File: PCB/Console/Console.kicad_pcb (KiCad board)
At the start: 2 copper layers, 9 parts, among them J1 Conn_01x04_Socket, J2 Conn_01x02_Socket, J3 Conn_01x08_Socket, J4 Conn_01x06, U1 WeMos D1 Mini32

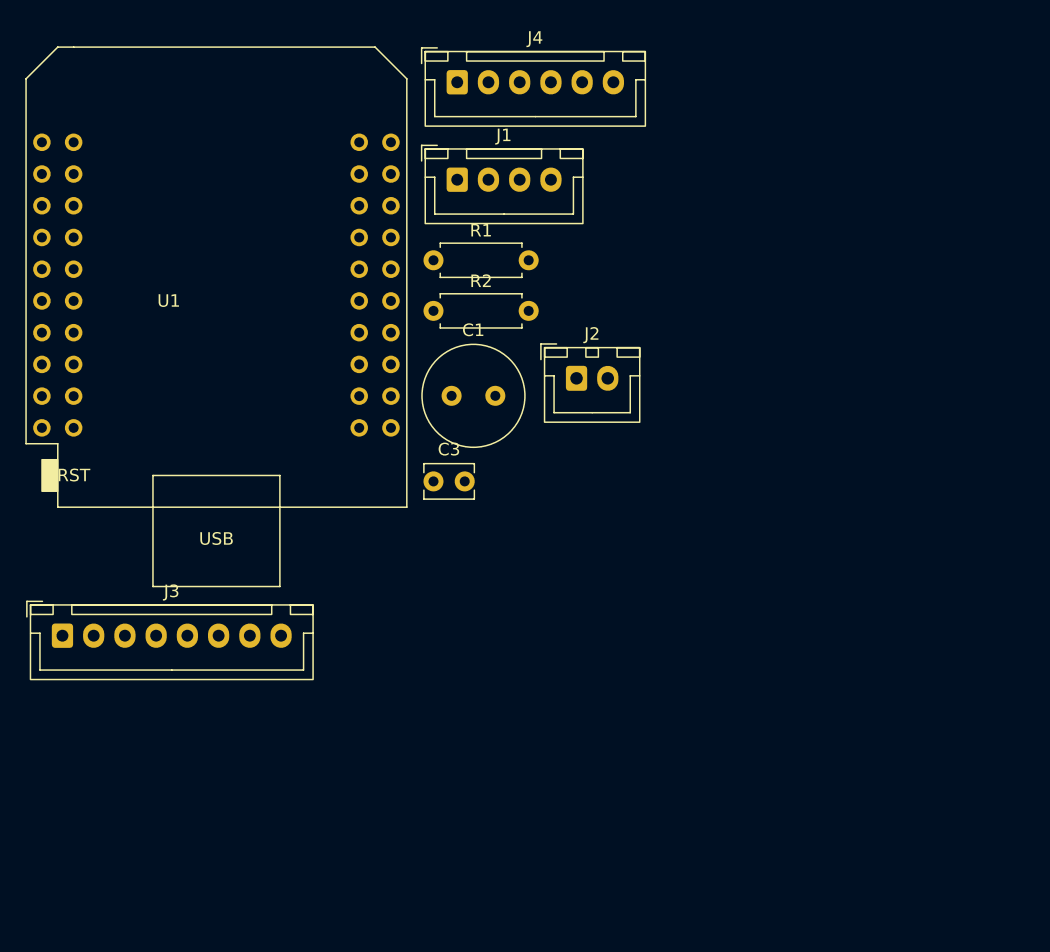
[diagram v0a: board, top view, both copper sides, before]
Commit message: Console: swap Waveshare pigtail for M128 7-pin socket (J3); F8 to PCB
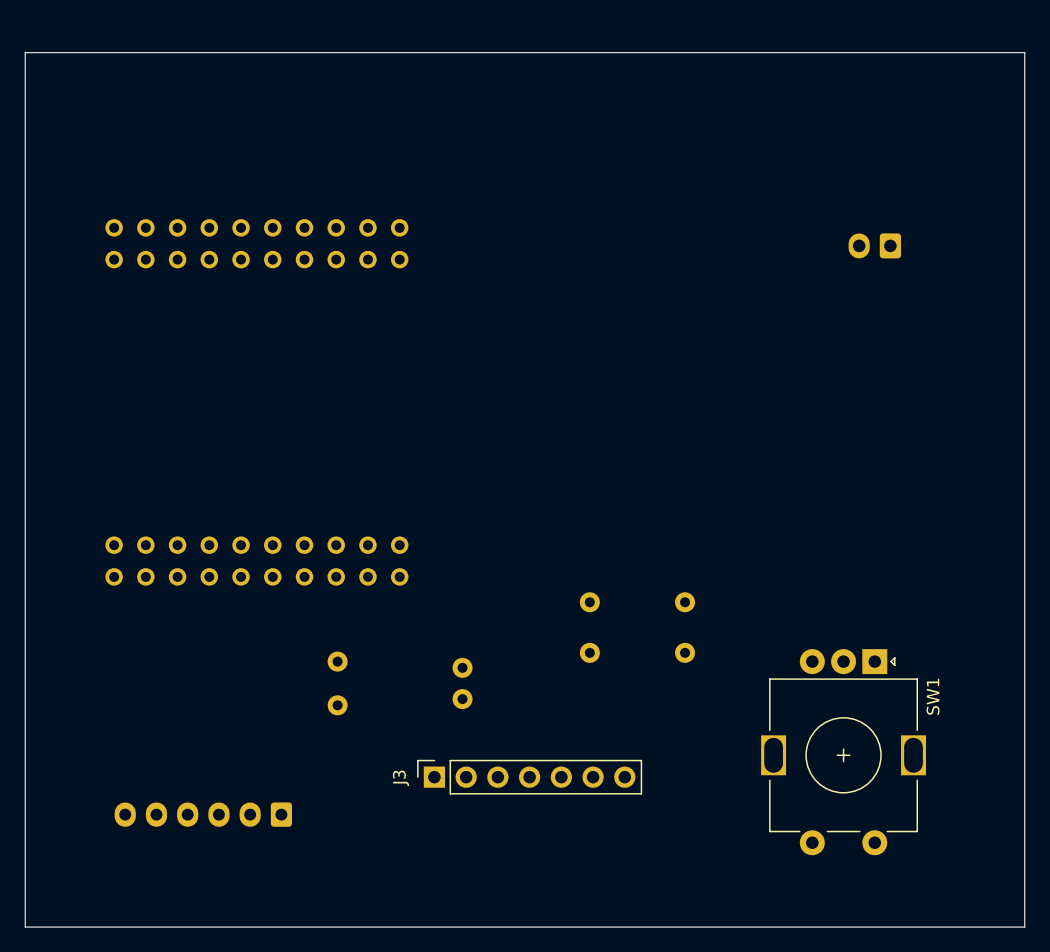
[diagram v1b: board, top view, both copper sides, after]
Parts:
- removed J1: Conn_01x04_Socket, Connector_JST:JST_XH_B4B-XH-A_1x04_P2.50mm_Vertical
- added SW1: RotaryEncoder_Switch_MP, Rotary_Encoder:RotaryEncoder_Alps_EC11E-Switch_Vertical_H20mm, F.Cu at (68.0, 48.8)
- C1, C3, J2, J4, R1, R2, U1: moved to B.Cu
- J3: value Conn_01x08_Socket -> Conn_01x07; footprint Connector_JST:JST_XH_B8B-XH-A_1x08_P2.50mm_Vertical -> Connector_PinSocket_2.54mm:PinSocket_1x07_P2.54mm_Vertical
- moved J4 60.3 mm to (20.5, 61.0), turned to 180 degrees
- moved R1 34.0 mm to (52.8, 44.0), turned to 180 degrees
- moved R2 34.0 mm to (52.8, 48.0), turned to 180 degrees
- moved J3 31.9 mm to (32.8, 58.0), turned to 90 degrees
- moved J2 27.3 mm to (69.2, 15.5), turned to 180 degrees
- moved C1 23.1 mm to (25.0, 48.8), turned to -90 degrees
- moved C3 15.1 mm to (35.0, 49.2), turned to -90 degrees
- moved U1 9.93 mm to (18.5, 28.0), turned to 90 degrees
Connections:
- J3 pad 1: GND -> /LCD_Vcc
- J3 pad 2: /LCD_Vcc -> GND
- J3 pad 5: /LCD_RST -> /LCD_DC
- J3 pad 6: /LCD_DC -> /LCD_CS
- J3 pad 7: /LCD_CS -> /LCD_RST
- U1 pad 29: /LCD_MISO -> unconnected-(U1-IO19-Pad29)
- U1 pad 8: /LCD_BackLt -> unconnected-(U1-IO21-Pad8)
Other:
- board outline added: 80 x 70 mm
